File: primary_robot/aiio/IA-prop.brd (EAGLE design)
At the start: 116 x 156 mm, 43 parts, among them U1 ARDUINO_R3_SHIELD

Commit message: [primary_robot] Fixes Uart2 to Uart1 on the BBB
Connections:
- removed net RX2_BBB: CON_I2C_UART.6, U$3.P9.22
- removed net TX2_BBB: CON_I2C_UART.5, U$3.P9.21
- new net RX1_BBB: CON_I2C_UART.6, U$3.P9.26
- new net TX1_BBB: CON_I2C_UART.5, U$3.P9.24
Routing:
- net TX1_BBB: track 0.00 -> 162.2 mm, vias 0 -> 2
- net RX2_BBB: track 158.6 -> 0.00 mm
- net RX1_BBB: track 0.00 -> 139.7 mm
- net TX2_BBB: track 101.9 -> 0.00 mm, vias 2 -> 0
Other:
- board text removed: "Convertisseur"
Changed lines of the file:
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@@
 <circle x="38.49" y="37.752" radius="1.5" width="1" layer="45"/>
 <circle x="37.22" y="-10.508" radius="1.5" width="1" layer="45"/>
-<text x="32.512" y="54.864" size="1.778" layer="16" rot="MR0">Convertisseur</text>
 <text x="2.794" y="96.774" size="1.016" layer="1" font="vector" ratio="15" rot="R90">GND</text>
 <text x="10.16" y="96.774" size="1.016" layer="1" font="vector" ratio="15" rot="R90">RX</text>
@@
 <wire x1="14.4246" y1="32.8194" x2="22.3608" y2="32.8194" width="1.016" layer="16"/>
 <wire x1="22.3608" y1="32.8194" x2="28.4568" y2="29.2634" width="1.016" layer="16"/>
-<wire x1="-32.44335" y1="61.564109375" x2="-33.02" y2="61.976" width="0" layer="19" extent="1-16"/>
 <wire x1="7.112" y1="15.748" x2="-8.89" y2="15.748" width="0.6096" layer="1"/>
 <wire x1="-8.89" y1="15.748" x2="-9.652" y2="15.494" width="0.6096" layer="1"/>
 <wire x1="-9.652" y1="15.494" x2="-18.034" y2="15.494" width="0.6096" layer="1"/>
+<wire x1="-32.44335" y1="61.564109375" x2="-33.02" y2="61.976" width="0" layer="19" extent="1-16"/>
 </signal>
 <signal name="N$4">
@@
 <wire x1="33.02" y1="16.002" x2="33.274" y2="16.256" width="1.016" layer="16"/>
 </signal>
-<signal name="TX2_BBB">
-<contactref element="U$3" pad="P9.21"/>
-<contactref element="CON_I2C_UART" pad="5"/>
-<wire x1="5.132" y1="87.273" x2="5.029" y2="84.836" width="0.8128" layer="16"/>
-<wire x1="5.029" y1="84.836" x2="7.62" y2="83.82" width="0.8128" layer="16"/>
-<wire x1="36.85" y1="12.934" x2="38.608" y2="16.256" width="1.016" layer="1"/>
-<wire x1="38.608" y1="50.292" x2="7.62" y2="83.82" width="1.016" layer="1"/>
-<via x="36.85" y="12.934" extent="1-16" drill="0.6" diameter="2.1844"/>
-<via x="7.62" y="83.82" extent="1-16" drill="0.6" diameter="2.1844"/>
-<wire x1="46.16" y1="13.95" x2="41.93" y2="13.95" width="1.016" layer="16"/>
-<wire x1="41.93" y1="13.95" x2="36.85" y2="12.934" width="1.016" layer="16"/>
-<wire x1="38.608" y1="16.256" x2="38.608" y2="29.972" width="1.016" layer="1"/>
-<wire x1="38.608" y1="29.972" x2="43.18" y2="34.544" width="1.016" layer="1"/>
-<wire x1="43.18" y1="34.544" x2="43.18" y2="45.72" width="1.016" layer="1"/>
-<wire x1="43.18" y1="45.72" x2="38.608" y2="50.292" width="1.016" layer="1"/>
-</signal>
-<signal name="RX2_BBB">
-<contactref element="U$3" pad="P9.22"/>
-<contactref element="CON_I2C_UART" pad="6"/>
-<wire x1="46.16" y1="11.41" x2="49.51" y2="11.45" width="0.8128" layer="16"/>
-<wire x1="49.51" y1="11.45" x2="56.388" y2="15.748" width="0.8128" layer="16"/>
-<wire x1="56.388" y1="15.748" x2="56.388" y2="87.884" width="0.8128" layer="16"/>
-<wire x1="56.388" y1="87.884" x2="46.269834375" y2="99.532140625" width="0.8128" layer="16"/>
-<wire x1="1.016" y1="91.44" x2="5.08" y2="91.44" width="0.4064" layer="16"/>
-<wire x1="5.08" y1="91.44" x2="5.132" y2="89.813" width="0.4064" layer="16"/>
-<wire x1="1.016" y1="91.44" x2="-0.508" y2="93.472" width="0.4064" layer="16"/>
-<wire x1="-0.508" y1="93.472" x2="-0.508" y2="97.536" width="1.016" layer="16"/>
-<wire x1="-0.508" y1="97.536" x2="3.561975" y2="99.568" width="1.016" layer="16"/>
-<wire x1="3.561975" y1="99.568" x2="46.269834375" y2="99.532140625" width="1.016" layer="16"/>
-</signal>
 <signal name="N$7">
 <contactref element="R3" pad="P$2"/>
@@
 <wire x1="110" y1="110" x2="110" y2="100" width="2.1844" layer="16"/>
 </signal>
+<signal name="TX1_BBB">
+<contactref element="U$3" pad="P9.24"/>
+<contactref element="CON_I2C_UART" pad="5"/>
+<wire x1="-0.559" y1="91.694" x2="-2.794" y2="93.726" width="0.8128" layer="16"/>
+<wire x1="36.85" y1="12.934" x2="38.608" y2="16.256" width="1.016" layer="1"/>
+<wire x1="36.83" y1="101.346" x2="-0.762" y2="101.346" width="1.016" layer="1"/>
+<wire x1="-0.762" y1="101.346" x2="-2.794" y2="99.314" width="1.016" layer="1"/>
+<wire x1="-2.794" y1="99.314" x2="-2.794" y2="93.726" width="1.016" layer="1"/>
+<via x="36.85" y="12.934" extent="1-16" drill="0.6" diameter="2.1844"/>
+<via x="-2.794" y="93.726" extent="1-16" drill="0.6" diameter="2.1844"/>
+<wire x1="46.16" y1="13.95" x2="41.93" y2="13.95" width="1.016" layer="16"/>
+<wire x1="41.93" y1="13.95" x2="36.85" y2="12.934" width="1.016" layer="16"/>
+<wire x1="38.608" y1="16.256" x2="38.608" y2="29.972" width="1.016" layer="1"/>
+<wire x1="38.608" y1="29.972" x2="42.164" y2="34.544" width="1.016" layer="1"/>
+<wire x1="42.164" y1="34.544" x2="42.164" y2="80.518" width="1.016" layer="1"/>
+<wire x1="42.164" y1="80.518" x2="44.196" y2="82.55" width="1.016" layer="1"/>
+<wire x1="44.196" y1="82.55" x2="44.196" y2="93.726" width="1.016" layer="1"/>
+<wire x1="44.196" y1="93.726" x2="36.83" y2="101.346" width="1.016" layer="1"/>
+<wire x1="-0.559" y1="91.694" x2="7.112" y2="91.694" width="0.4064" layer="16"/>
+<wire x1="7.112" y1="91.694" x2="7.62" y2="91.186" width="0.4064" layer="16"/>
+<wire x1="7.62" y1="91.186" x2="7.62" y2="89.865" width="0.4064" layer="16"/>
+<wire x1="7.62" y1="89.865" x2="7.672" y2="89.813" width="0.4064" layer="16"/>
+</signal>
+<signal name="RX1_BBB">
+<contactref element="U$3" pad="P9.26"/>
+<contactref element="CON_I2C_UART" pad="6"/>
+<wire x1="46.16" y1="11.41" x2="49.51" y2="11.45" width="0.8128" layer="16"/>
+<wire x1="49.51" y1="11.45" x2="56.388" y2="15.748" width="0.8128" layer="16"/>
+<wire x1="56.388" y1="15.748" x2="56.388" y2="91.694" width="0.8128" layer="16"/>
+<wire x1="56.388" y1="91.694" x2="51.054" y2="97.028" width="0.8128" layer="16"/>
+<wire x1="51.054" y1="97.028" x2="22.352" y2="97.028" width="0.8128" layer="16"/>
+<wire x1="22.352" y1="97.028" x2="17.018" y2="91.694" width="0.8128" layer="16"/>
+<wire x1="17.018" y1="91.694" x2="10.668" y2="91.694" width="0.4064" layer="16"/>
+<wire x1="10.668" y1="91.694" x2="10.16" y2="91.186" width="0.4064" layer="16"/>
+<wire x1="10.16" y1="91.186" x2="10.16" y2="89.865" width="0.4064" layer="16"/>
+<wire x1="10.16" y1="89.865" x2="10.212" y2="89.813" width="0.4064" layer="16"/>
+</signal>
 </signals>

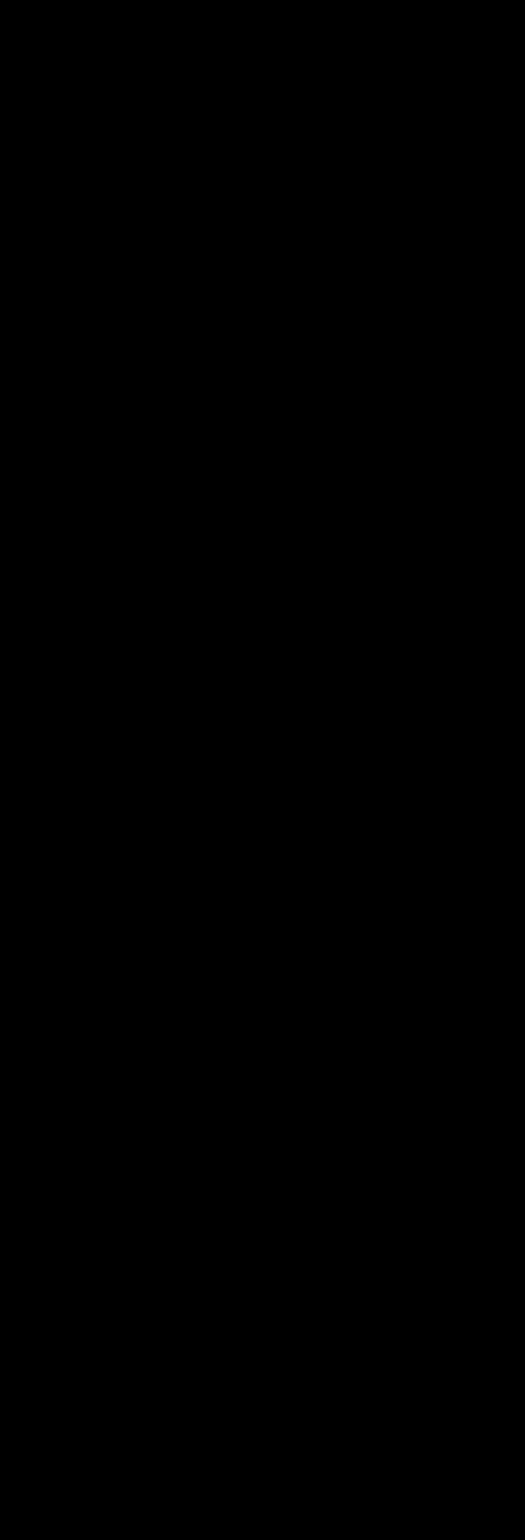
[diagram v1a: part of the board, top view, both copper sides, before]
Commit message: [AIIO_board] Add I2C bus "I2C0" for sonar sensors on shematic file.
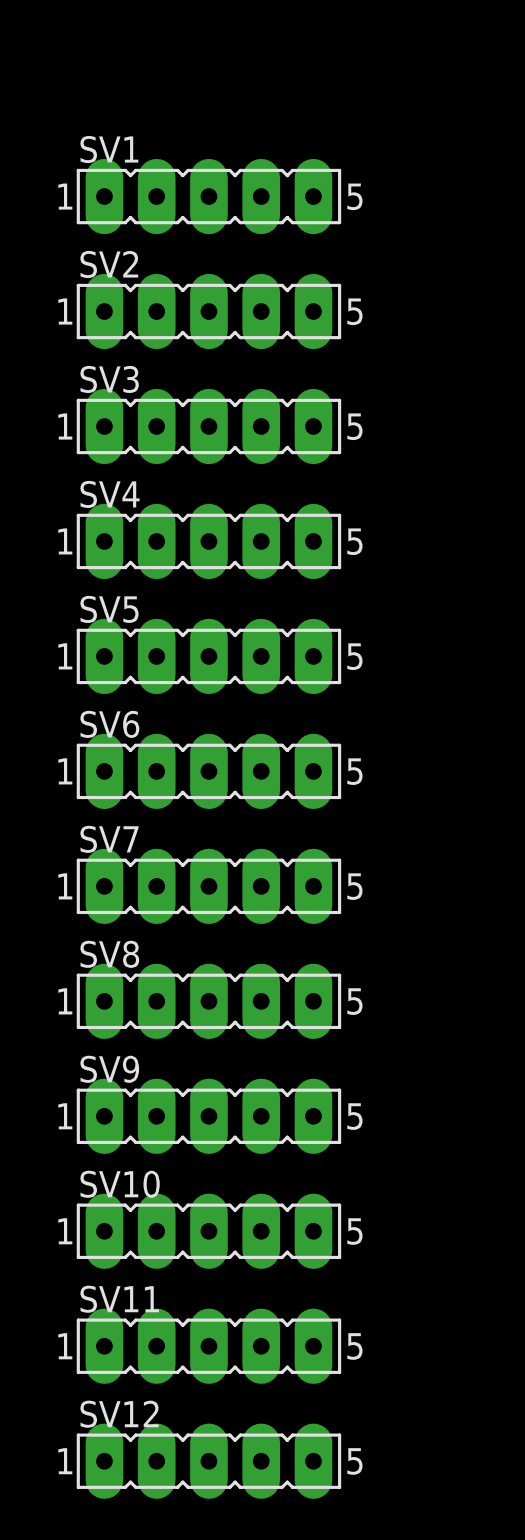
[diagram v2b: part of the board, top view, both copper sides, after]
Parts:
- added SV1, SV10, SV11, SV12, SV2, SV3, SV4, SV5, SV6, SV7, SV8, SV9: (no value), con-lsta:FE05-1
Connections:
- new net N$10: SV1.2, SV10.2, SV11.2, SV12.2, SV2.2, SV3.2, SV4.2, SV5.2, SV6.2, SV7.2, SV8.2, SV9.2
- new net N$11: SV1.3, SV10.3, SV11.3, SV12.3, SV2.3, SV3.3, SV4.3, SV5.3, SV6.3, SV7.3, SV8.3, SV9.3
- new net N$12: SV1.4, SV10.4, SV11.4, SV12.4, SV2.4, SV3.4, SV4.4, SV5.4, SV6.4, SV7.4, SV8.4, SV9.4
- new net N$13: SV1.5, SV10.5, SV12.5, SV3.5, SV4.5, SV6.5, SV7.5, SV9.5
- new net N$23: SV5.5
- new net N$38: SV8.5
- new net N$48: SV2.5
- new net N$6: SV1.1, SV10.1, SV11.1, SV12.1, SV2.1, SV3.1, SV4.1, SV5.1, SV6.1, SV7.1, SV8.1, SV9.1
- new net N$63: SV11.5
